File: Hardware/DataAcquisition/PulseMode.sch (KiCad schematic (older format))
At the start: 21 parts, among them Q4 Q_NJFET_DGS, Q5 Q_NJFET_DGS, U2 LM358, U7 Opamp_Dual_Generic

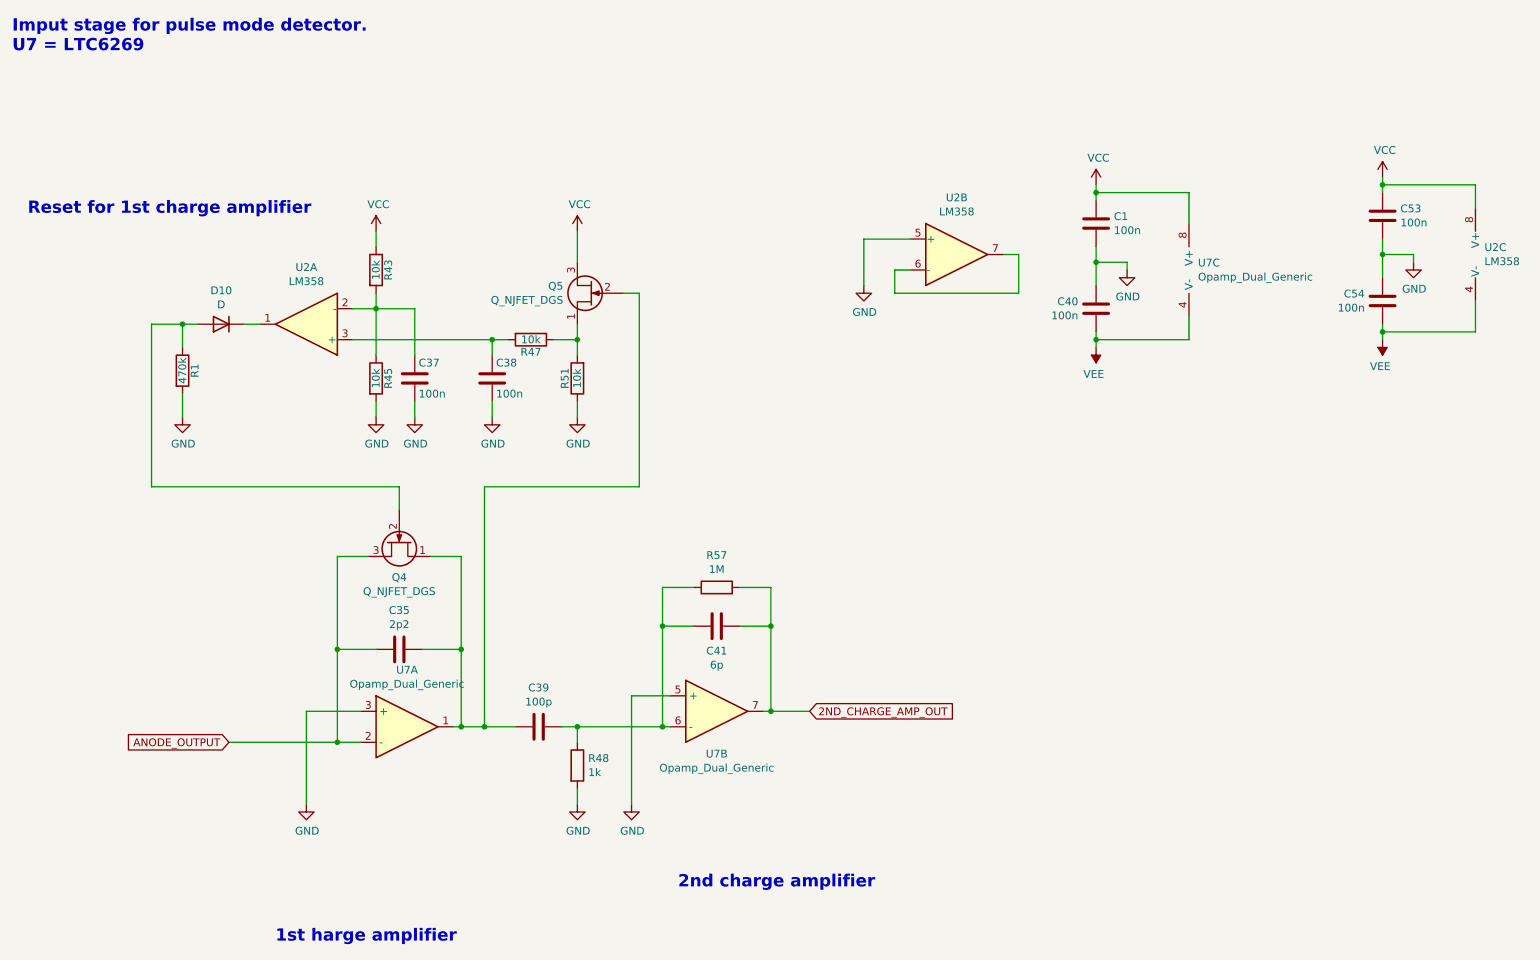
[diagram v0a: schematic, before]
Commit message: split (previousle one) pcb project to three separate pcbs
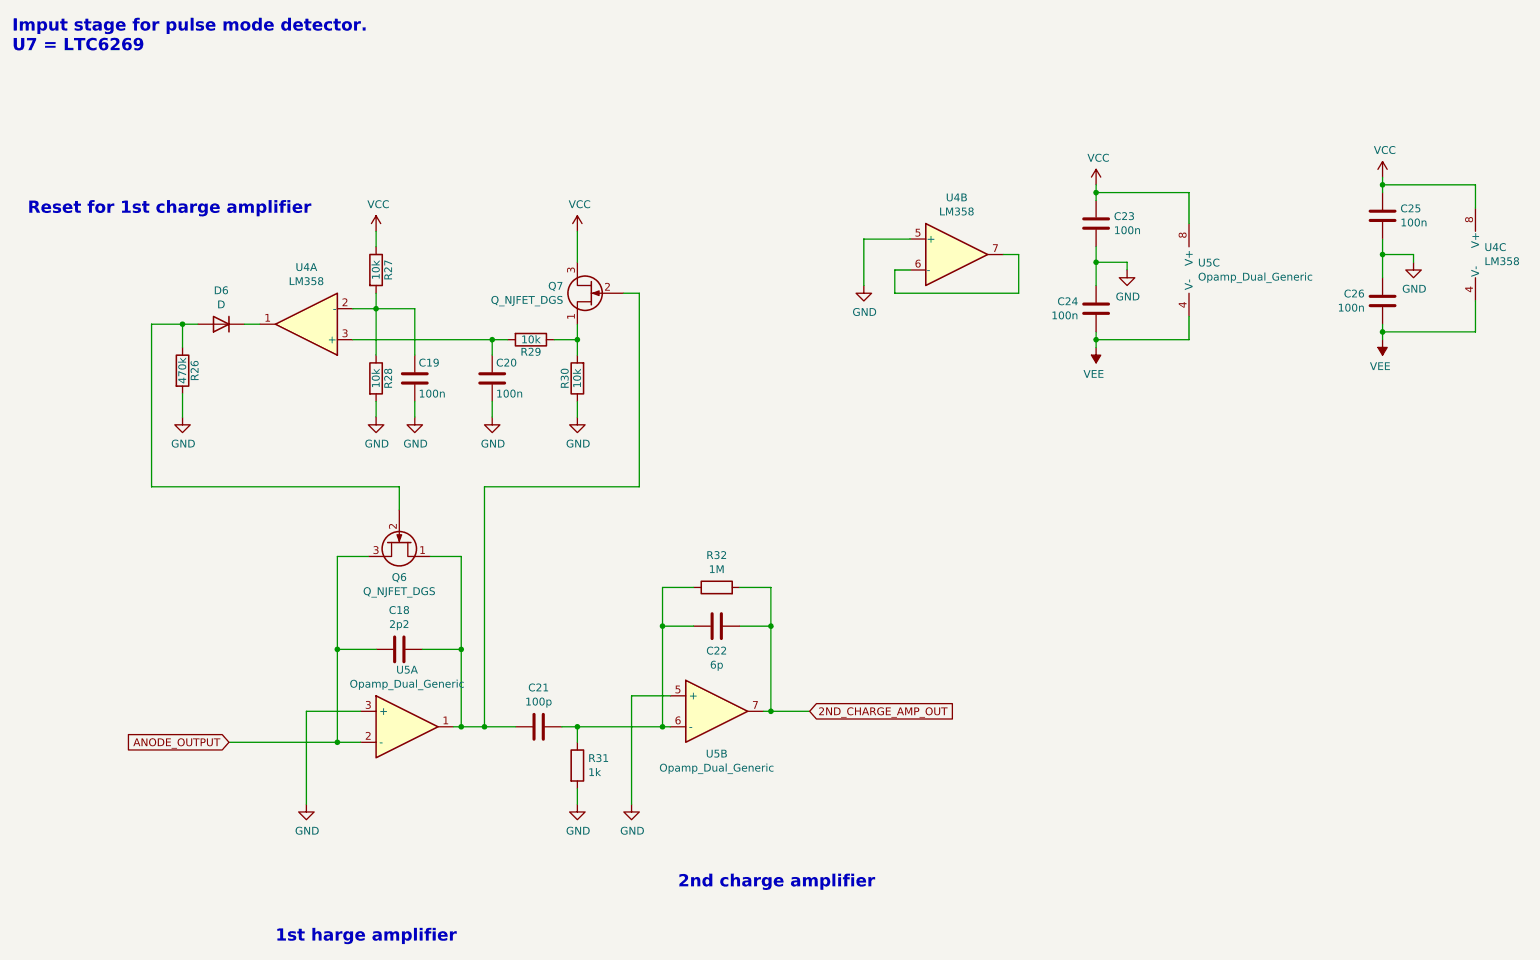
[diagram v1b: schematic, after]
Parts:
- renumbered C35 to C18, C37 to C19, C38 to C20, C39 to C21, C41 to C22, C1 to C23, C40 to C24, C53 to C25, C54 to C26, D10 to D6, Q4 to Q6, Q5 to Q7, R1 to R26, R43 to R27, R45 to R28, R47 to R29, R51 to R30, R48 to R31, R57 to R32, U2 to U4, U7 to U5
